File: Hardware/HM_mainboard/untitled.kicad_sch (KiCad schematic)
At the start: 15 parts, among them Q1 MOSFET-PCHANNELDMG2307L, U2 V_REG_LDOSMD, U3 MCP73831

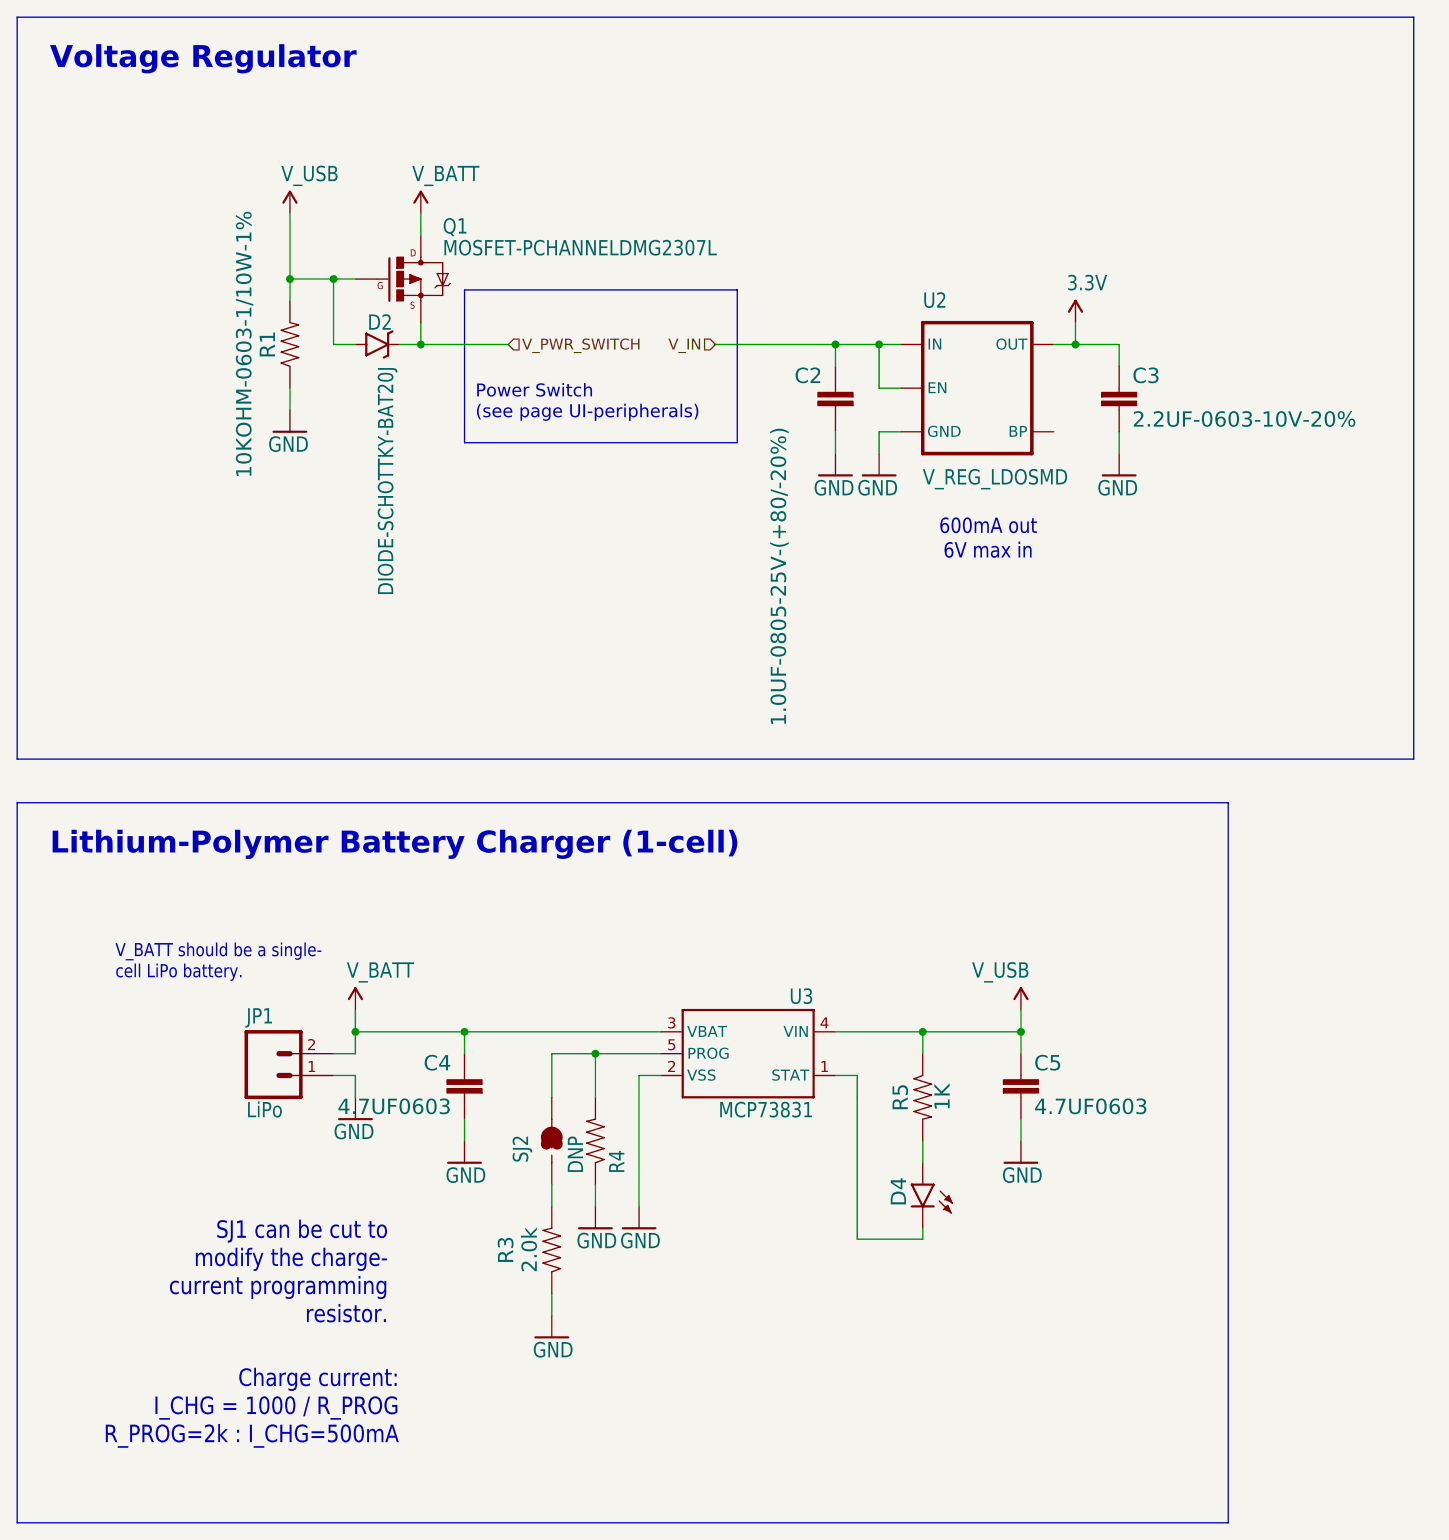
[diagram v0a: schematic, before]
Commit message: Updated components of power supply unit
- Replaced PMOSFET
- Replaced LDO
- Replaced battery charger
- Replaced caps and resistors
- Replaced battery connector
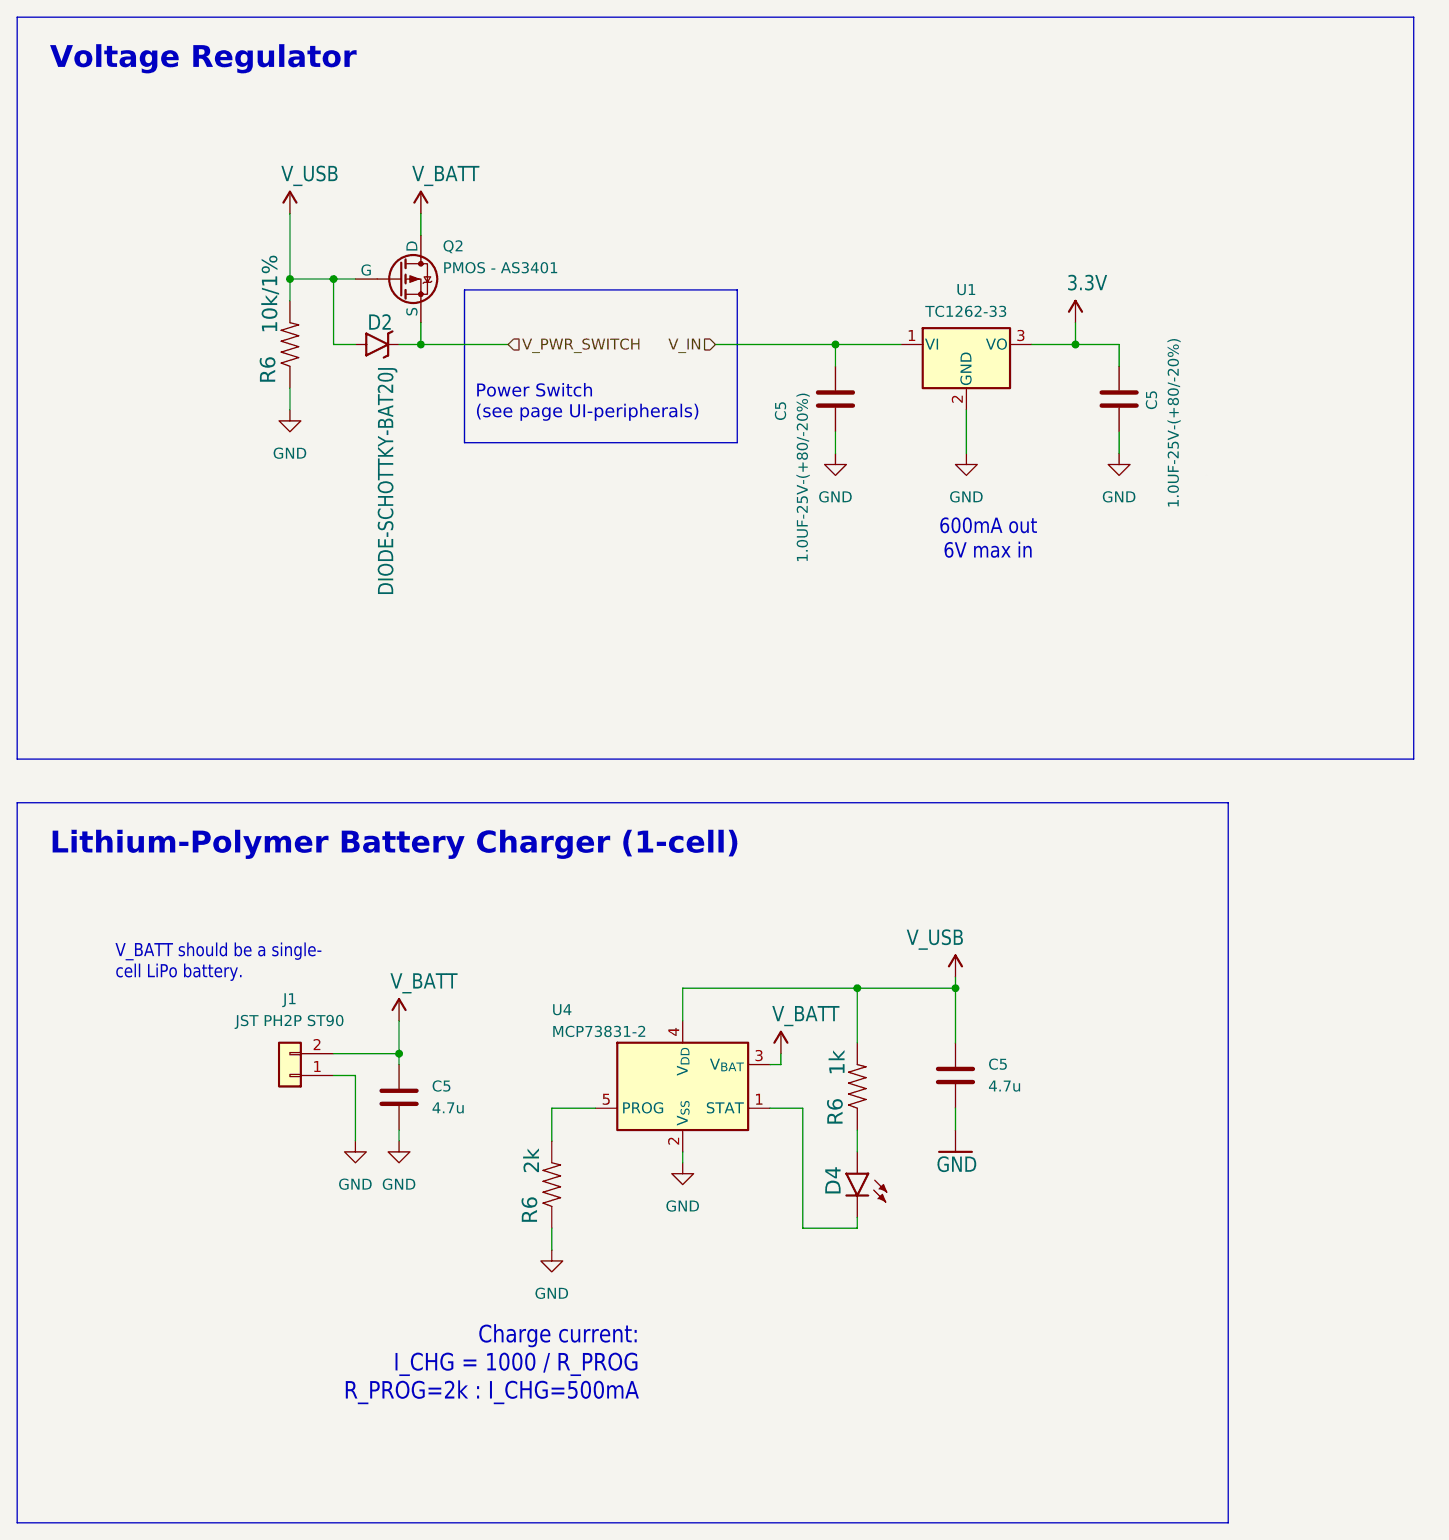
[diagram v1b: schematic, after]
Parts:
- removed C2: 1.0UF-0805-25V-(+80/-20%), esp32-thing:0805, symbol esp32-thing-eagle-import:1.0UF-0805-25V-(+80/-20%)
- removed C3: 2.2UF-0603-10V-20%, esp32-thing:0603, symbol esp32-thing-eagle-import:2.2UF-0603-10V-20%
- removed C4, C5: 4.7UF0603, esp32-thing:0603, symbol esp32-thing-eagle-import:4.7UF0603
- removed JP1: LiPo, esp32-thing:JST-2-PTH, symbol esp32-thing-eagle-import:M02JST-PTH-2
- removed Q1: MOSFET-PCHANNELDMG2307L, esp32-thing:SOT23-3, symbol esp32-thing-eagle-import:MOSFET-PCHANNELDMG2307L
- removed R1: 10KOHM-0603-1/10W-1%, esp32-thing:0603, symbol esp32-thing-eagle-import:10KOHM-0603-1/10W-1%
- removed R3: 2.0k, esp32-thing:0603, symbol esp32-thing-eagle-import:2.0KOHM1/10W5%(0603)
- removed R4: DNP, esp32-thing:1_6W-RES, symbol esp32-thing-eagle-import:RESISTORPTH-1/6W
- removed R5: 1K, esp32-thing:0603, symbol esp32-thing-eagle-import:1KOHM-1/10W-1%(0603)
- removed SJ2: JUMPER-PAD-2-NC_BY_TRACE, esp32-thing:PAD-JUMPER-2-NC_BY_TRACE_YES_SILK, symbol esp32-thing-eagle-import:JUMPER-PAD-2-NC_BY_TRACE
- removed U2: V_REG_LDOSMD, esp32-thing:SOT23-5, symbol esp32-thing-eagle-import:V_REG_LDOSMD
- removed U3: MCP73831, esp32-thing:SOT23-5, symbol esp32-thing-eagle-import:MCP73831
- added C5 (x2): 1.0UF-25V-(+80/-20%), Capacitor_SMD:C_0603_1608Metric_Pad1.08x0.95mm_HandSolder, symbol Device:C
- added C5 (x2): 4.7u, Capacitor_SMD:C_0201_0603Metric_Pad0.64x0.40mm_HandSolder, symbol Device:C
- added J1: JST PH2P ST90, Connector_JST:JST_PH_S2B-PH-K_1x02_P2.00mm_Horizontal, symbol Connector_Generic:Conn_01x02
- added Q2: PMOS - AS3401, Package_TO_SOT_SMD:SOT-23, symbol Simulation_SPICE:PMOS
- added R6: 2k, Resistor_SMD:R_0201_0603Metric_Pad0.64x0.40mm_HandSolder, symbol esp32-thing-eagle-import:27OHM1/10W1%(0603)0603-RES
- added R6: 10k/1%, Resistor_SMD:R_0201_0603Metric_Pad0.64x0.40mm_HandSolder, symbol esp32-thing-eagle-import:27OHM1/10W1%(0603)0603-RES
- added R6: 1k, Resistor_SMD:R_0201_0603Metric_Pad0.64x0.40mm_HandSolder, symbol esp32-thing-eagle-import:27OHM1/10W1%(0603)0603-RES
- added U1: TC1262-33, Package_TO_SOT_SMD:SOT-223-3_TabPin2, symbol Regulator_Linear:TC1262-33
- added U4: MCP73831-2, Package_TO_SOT_SMD:SOT-23-5, symbol Battery_Management:MCP73831-2-OT
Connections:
- net 3.3V: now also C5.1, U1.3 (VO)
- net GND: now also C5.2, C5.2, C5.2, C5.2, J1.1 (Pin_1), R6.1, R6.1, U1.2 (GND), U4.2 (V_{SS})
- net V_BATT: now also C5.1, J1.2 (Pin_2), Q2.1 (D), U4.3 (V_{BAT})
- net V_IN: now also C5.1, U1.1 (VI)
- net V_PWR_SWITCH: now also Q2.3 (S)
- net V_USB: now also C5.1, Q2.2 (G), R6.2, R6.2, U4.4 (V_{DD})
- net at D4.A: now also R6.1
- net at D4.C: now also U4.1 (STAT)
- new net: R6.2, U4.5 (PROG)
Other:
- note removed: "SJ1 can be cut to modify the charge- current programming resistor."
- moved on the sheet: D4
